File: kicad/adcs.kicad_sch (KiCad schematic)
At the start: 0 parts

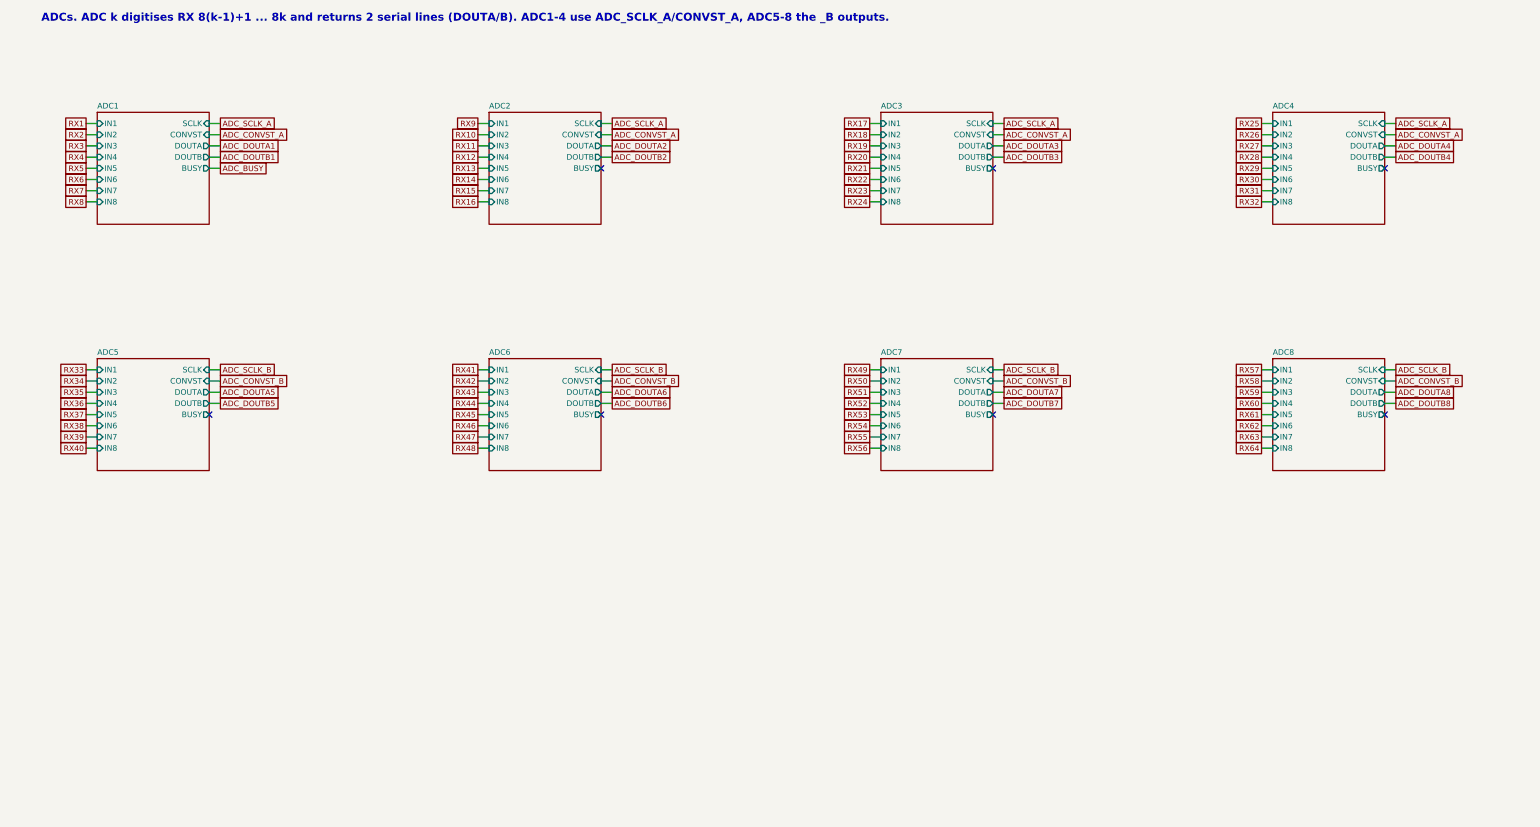
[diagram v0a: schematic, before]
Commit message: Switch to 16 x TLV320ADC5140, +3V3A rail, 3 A buck, datasheet library, transducer DNP
- ADC: 8 x AD7606C-16 ($470/board) -> 16 x TI TLV320ADC5140 at 192 kSPS ($50/board): TDM slave on a
  shared BCLK/FSYNC, I2C (SCL + 4 SDA groups), 2k/1k + 100 nF input network; project symbol from
  scripts/make_symbols.py; 9 clock buffers; J2 remapped
- power: +3V3A (second TPS7A4700, ANY-OUT 3.3 V); +5V buck TPS54202 -> TPS54302 (3 A), L1 10 uH 5 A
- checks and simulations updated for the new ADC input (all 18 checks and 10 sims pass)
- docs/datasheets: a PDF for every part, kept in step by scripts/datasheets.py (run by bom.py)
- design brief section 5a: interface bandwidth budget (no bus is a bottleneck; TX_EDGE = 1)
- CUSA-TR65 marked DNP for JLCPCB (hand-soldered), priced at DigiKey 100+
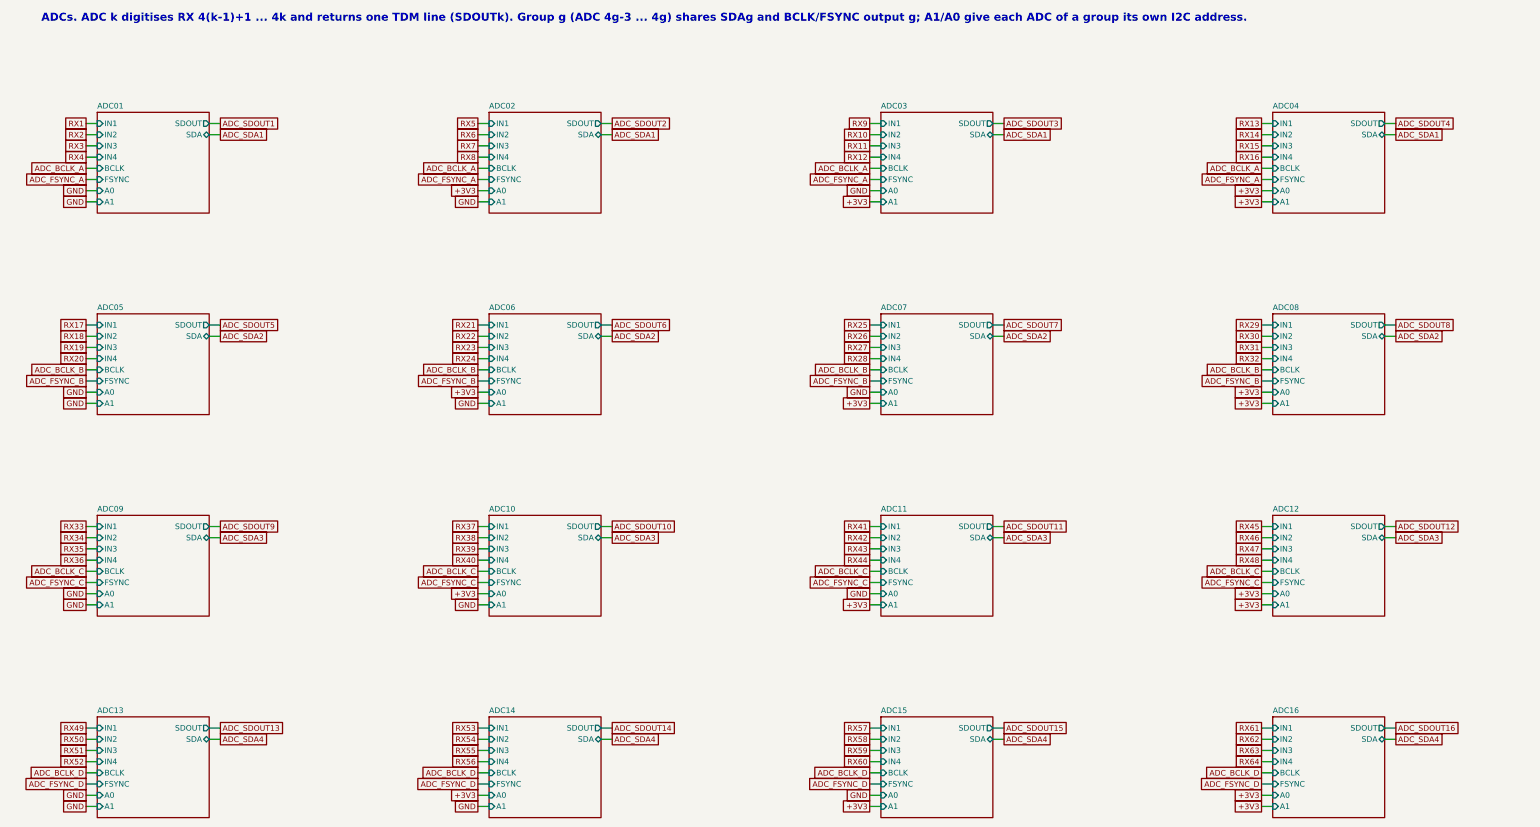
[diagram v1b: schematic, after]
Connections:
- no-connect marks 7 -> 0
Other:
- removed sheet ADC1
- removed sheet ADC2
- removed sheet ADC3
- removed sheet ADC4
- removed sheet ADC5
- removed sheet ADC6
- removed sheet ADC7
- removed sheet ADC8
- added sheet ADC01 (adc.kicad_sch)
- added sheet ADC02 (adc.kicad_sch)
- added sheet ADC03 (adc.kicad_sch)
- added sheet ADC04 (adc.kicad_sch)
- added sheet ADC05 (adc.kicad_sch)
- added sheet ADC06 (adc.kicad_sch)
- added sheet ADC07 (adc.kicad_sch)
- added sheet ADC08 (adc.kicad_sch)
- added sheet ADC09 (adc.kicad_sch)
- added sheet ADC10 (adc.kicad_sch)
- added sheet ADC11 (adc.kicad_sch)
- added sheet ADC12 (adc.kicad_sch)
- added sheet ADC13 (adc.kicad_sch)
- added sheet ADC14 (adc.kicad_sch)
- added sheet ADC15 (adc.kicad_sch)
- added sheet ADC16 (adc.kicad_sch)
- note added: "ADCs. ADC k digitises RX 4(k-1)+1 ... 4k and returns one TDM line (SDOUTk). Group g (ADC 4g-3 ... 4g) shares SDAg and BCLK/FSYNC output g; A1/A0 give each ADC of a group its own I2C address."
- note removed: "ADCs. ADC k digitises RX 8(k-1)+1 ... 8k and returns 2 serial lines (DOUTA/B). ADC1-4 use ADC_SCLK_A/CONVST_A, ADC5-8 the _B outputs."
- title: ADCs: 8 x AD7606C-16 -> ADCs: 16 x TLV320ADC5140 (4 channels each)
